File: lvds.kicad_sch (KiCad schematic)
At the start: 31 parts, among them J9 Conn_01x34_Female, U10 TPS61177A, U11 TCA9802, U12 NTB0102, U13 MIC5504-1.8YM5, U5 SN65DSI83TPAPRQ1

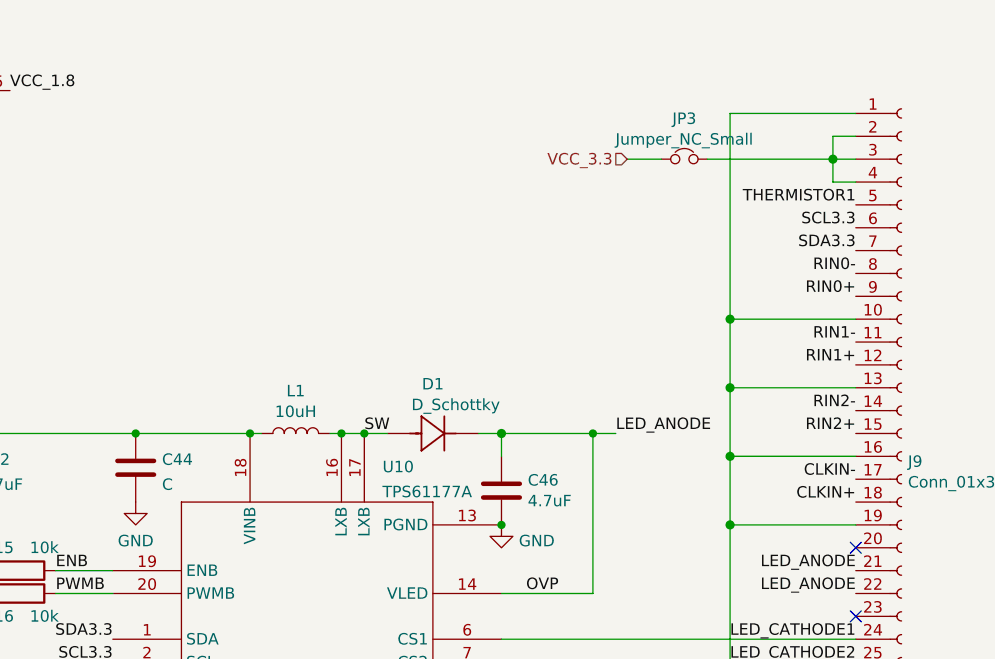
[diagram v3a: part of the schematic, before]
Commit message: Route remaining signals after rotating CM4
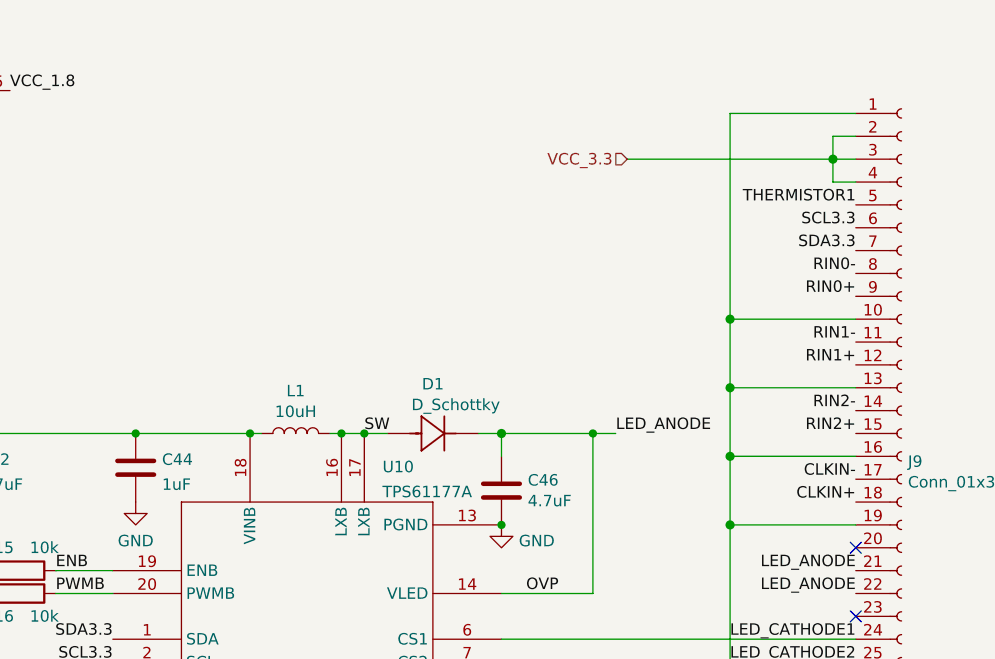
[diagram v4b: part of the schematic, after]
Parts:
- removed JP3: Jumper_NC_Small, Resistor_SMD:R_0402_1005Metric, symbol Device:Jumper_NC_Small
- C44: value C -> 1uF
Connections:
- net VCC_3.3: now also J9.2 (Pin_2), J9.3 (Pin_3), J9.4 (Pin_4)
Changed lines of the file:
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@@
-    (stroke (width 0) (type solid) (color 0 0 0 0))
-  )
-  (wire (pts (xy 236.22 34.29) (xy 240.03 34.29))
     (stroke (width 0) (type solid) (color 0 0 0 0))
   )
@@
     (stroke (width 0) (type solid) (color 0 0 0 0))
   )
-  (wire (pts (xy 245.11 34.29) (xy 259.08 34.29))
+  (wire (pts (xy 236.22 34.29) (xy 259.08 34.29))
     (stroke (width 0) (type solid) (color 0 0 0 0))
   )
@@
     )
     (property "Datasheet" "~" (id 3) (at 222.25 71.12 0)
-      (effects (font (size 1.27 1.27)) hide)
-    )
-    (pin "1")
-    (pin "2")
-  )
-  (symbol (lib_id "Device:Jumper_NC_Small") (at 242.57 34.29 0) (unit 1)
-    (in_bom yes) (on_board yes) (fields_autoplaced)
-    (property "Reference" "JP3" (id 0) (at 242.57 29.79 0))
-    (property "Value" "Jumper_NC_Small" (id 1) (at 242.57 32.0887 0))
-    (property "Footprint" "Resistor_SMD:R_0402_1005Metric" (id 2) (at 242.57 34.29 0)
-      (effects (font (size 1.27 1.27)) hide)
-    )
-    (property "Datasheet" "~" (id 3) (at 242.57 34.29 0)
       (effects (font (size 1.27 1.27)) hide)
     )
@@
       (effects (font (size 1.27 1.27)) (justify left))
     )
-    (property "Value" "C" (id 1) (at 184.531 70.4466 0)
-      (effects (font (size 1.27 1.27)) (justify left))
-    )
+    (property "Value" "1uF" (id 1) (at 184.531 70.4466 0)
+      (effects (font (size 1.27 1.27)) (justify left))
+    )

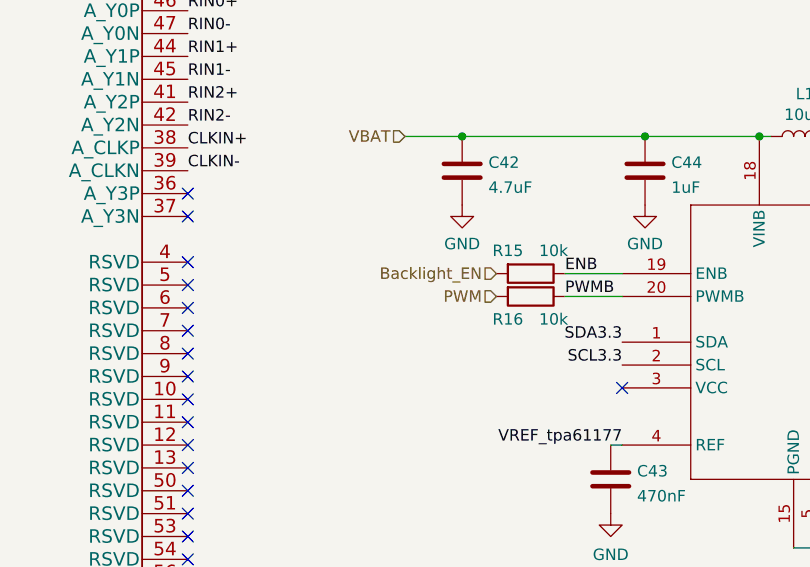
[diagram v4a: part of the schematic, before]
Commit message: Lots of tiny test points; add 3d models to a bunch of things. Re-length-match PCIe and DSI traces.
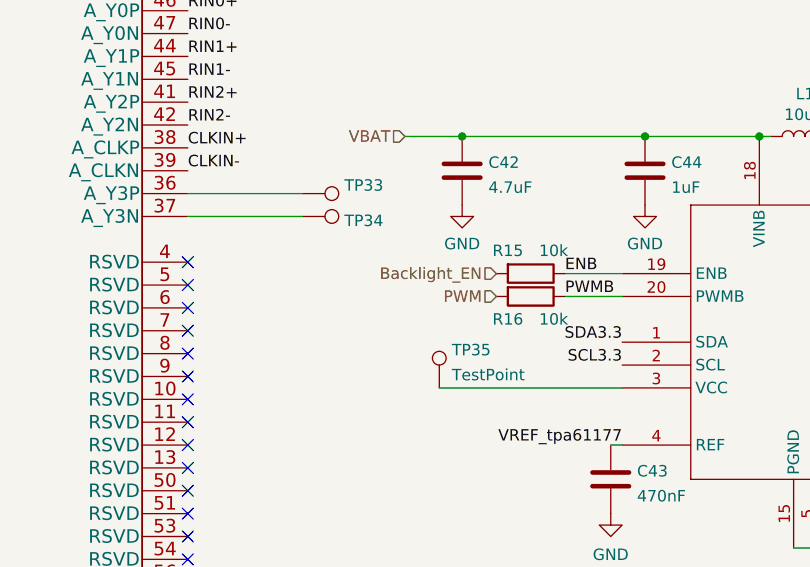
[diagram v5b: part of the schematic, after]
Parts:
- added TP33, TP34, TP35: TestPoint, footprints:testpoint_small, symbol Connector:TestPoint
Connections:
- net at U10.3 (VCC): now also TP35.1
- net at U5.36 (A_Y3P): now also TP33.1
- net at U5.37 (A_Y3N): now also TP34.1
- no-connect marks 28 -> 25
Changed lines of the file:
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@@
   (no_connect (at 130.81 124.46))
   (no_connect (at 130.81 127))
-  (no_connect (at 179.07 92.71))
   (no_connect (at 90.17 137.16))
   (no_connect (at 90.17 139.7))
   (no_connect (at 261.62 77.47))
   (no_connect (at 26.67 125.73))
-  (no_connect (at 130.81 71.12))
-  (no_connect (at 130.81 73.66))
   (wire (pts (xy 201.93 110.49) (xy 203.2 110.49))
     (stroke (width 0) (type default) (color 0 0 0 0))
@@
     (stroke (width 0) (type solid) (color 0 0 0 0))
   )
+  (wire (pts (xy 130.81 71.12) (xy 143.51 71.12))
+    (stroke (width 0) (type default) (color 0 0 0 0))
+  )
   (wire (pts (xy 232.41 64.77) (xy 232.41 82.55))
     (stroke (width 0) (type solid) (color 0 0 0 0))
@@
     (stroke (width 0) (type default) (color 0 0 0 0))
   )
+  (wire (pts (xy 158.75 92.71) (xy 179.07 92.71))
+    (stroke (width 0) (type default) (color 0 0 0 0))
+  )
   (wire (pts (xy 161.29 64.77) (xy 181.61 64.77))
     (stroke (width 0) (type default) (color 0 0 0 0))
@@
     (stroke (width 0) (type solid) (color 0 0 0 0))
   )
+  (wire (pts (xy 130.81 73.66) (xy 143.51 73.66))
+    (stroke (width 0) (type default) (color 0 0 0 0))
+  )
   (wire (pts (xy 201.93 110.49) (xy 201.93 113.03))
     (stroke (width 0) (type default) (color 0 0 0 0))
@@
     (pin "1")
     (pin "2")
+  )
+  (symbol (lib_id "Connector:TestPoint") (at 143.51 71.12 270) (unit 1)
+    (in_bom yes) (on_board yes)
+    (property "Reference" "TP33" (id 0) (at 148.209 70.2115 90)
+      (effects (font (size 1.27 1.27)) (justify left))
+    )
+    (property "Value" "TestPoint" (id 1) (at 152.4 69.85 90)
+      (effects (font (size 1.27 1.27)) (justify left) hide)
+    )
+    (property "Footprint" "footprints:testpoint_small" (id 2) (at 143.51 76.2 0)
+      (effects (font (size 1.27 1.27)) hide)
+    )
+    (property "Datasheet" "~" (id 3) (at 143.51 76.2 0)
+      (effects (font (size 1.27 1.27)) hide)
+    )
+    (pin "1")
   )
   (symbol (lib_id "Device:C") (at 35.56 25.4 0) (unit 1)
@@
     (pin "1")
   )
+  (symbol (lib_id "Connector:TestPoint") (at 158.75 92.71 0) (unit 1)
+    (in_bom yes) (on_board yes) (fields_autoplaced)
+    (property "Reference" "TP35" (id 0) (at 160.147 88.4995 0)
+      (effects (font (size 1.27 1.27)) (justify left))
+    )
+    (property "Value" "TestPoint" (id 1) (at 160.147 91.2746 0)
+      (effects (font (size 1.27 1.27)) (justify left))
+    )
+    (property "Footprint" "footprints:testpoint_small" (id 2) (at 163.83 92.71 0)
+      (effects (font (size 1.27 1.27)) hide)
+    )
+    (property "Datasheet" "~" (id 3) (at 163.83 92.71 0)
+      (effects (font (size 1.27 1.27)) hide)
+    )
+    (pin "1")
+  )
   (symbol (lib_id "power:GND") (at 181.61 72.39 0) (unit 1)
     (in_bom yes) (on_board yes) (fields_autoplaced)
@@
       (effects (font (size 1.27 1.27)) hide)
     )
-    (property "Datasheet" "" (id 3) (at 201.93 87.63 0)
+    (property "Datasheet" "${KIPRJMOD}/datasheets/tps61177a.pdf" (id 3) (at 201.93 87.63 0)
       (effects (font (size 1.27 1.27)) hide)
     )
@@
     (pin "2")
   )
+  (symbol (lib_id "Connector:TestPoint") (at 143.51 73.66 270) (unit 1)
+    (in_bom yes) (on_board yes) (fields_autoplaced)
+    (property "Reference" "TP34" (id 0) (at 148.209 74.139 90)
+      (effects (font (size 1.27 1.27)) (justify left))
+    )
+    (property "Value" "TestPoint" (id 1) (at 148.209 75.5266 90)
+      (effects (font (size 1.27 1.27)) (justify left) hide)
+    )
+    (property "Footprint" "footprints:testpoint_small" (id 2) (at 143.51 78.74 0)
+      (effects (font (size 1.27 1.27)) hide)
+    )
+    (property "Datasheet" "~" (id 3) (at 143.51 78.74 0)
+      (effects (font (size 1.27 1.27)) hide)
+    )
+    (pin "1")
+  )
   (symbol (lib_id "power:GND") (at 77.47 29.21 0) (unit 1)

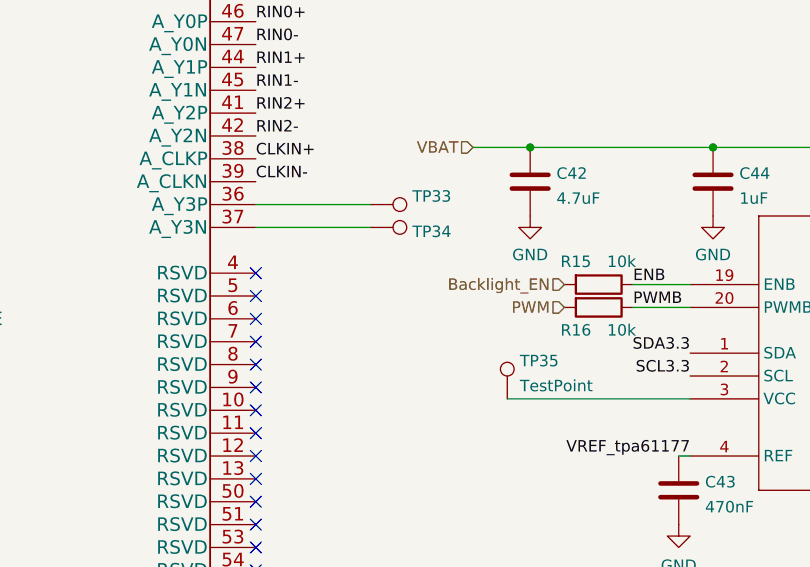
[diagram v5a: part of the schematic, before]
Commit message: Add a bunch more 3d models
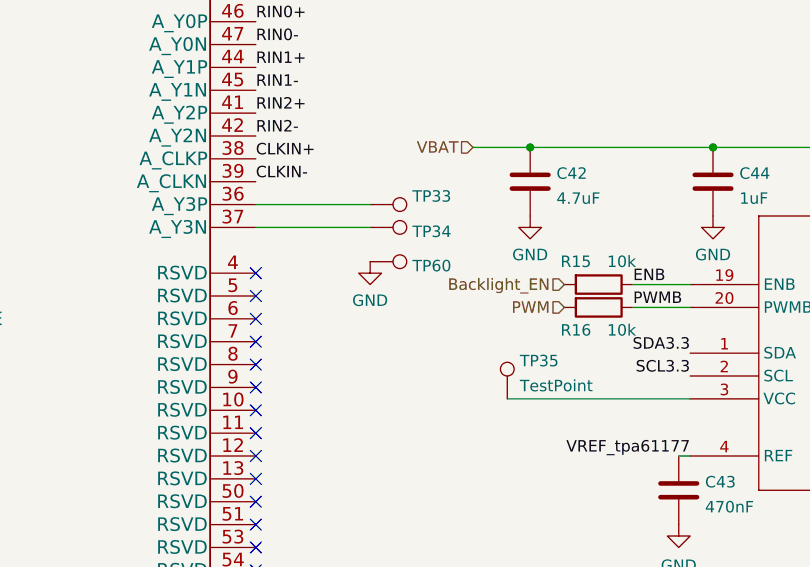
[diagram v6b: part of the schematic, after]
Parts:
- added TP60: TestPoint, footprints:testpoint_small, symbol Connector:TestPoint
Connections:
- net GND: now also TP60.1
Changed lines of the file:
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@@
     (pin "2")
+  )
+  (symbol (lib_id "Connector:TestPoint") (at 143.51 77.47 270) (unit 1)
+    (in_bom yes) (on_board yes) (fields_autoplaced)
+    (property "Reference" "TP60" (id 0) (at 148.209 77.949 90)
+      (effects (font (size 1.27 1.27)) (justify left))
+    )
+    (property "Value" "TestPoint" (id 1) (at 148.209 79.3366 90)
+      (effects (font (size 1.27 1.27)) (justify left) hide)
+    )
+    (property "Footprint" "footprints:testpoint_small" (id 2) (at 143.51 82.55 0)
+      (effects (font (size 1.27 1.27)) hide)
+    )
+    (property "Datasheet" "~" (id 3) (at 143.51 82.55 0)
+      (effects (font (size 1.27 1.27)) hide)
+    )
+    (pin "1")
   )
   (symbol (lib_id "Device:C") (at 96.52 25.4 0) (unit 1)
@@
     (pin "9")
   )
+  (symbol (lib_id "power:GND") (at 143.51 77.47 0) (unit 1)
+    (in_bom yes) (on_board yes) (fields_autoplaced)
+    (property "Reference" "#PWR030" (id 0) (at 143.51 83.82 0)
+      (effects (font (size 1.27 1.27)) hide)
+    )
+    (property "Value" "GND" (id 1) (at 143.51 81.7944 0))
+    (property "Footprint" "" (id 2) (at 143.51 77.47 0)
+      (effects (font (size 1.27 1.27)) hide)
+    )
+    (property "Datasheet" "" (id 3) (at 143.51 77.47 0)
+      (effects (font (size 1.27 1.27)) hide)
+    )
+    (pin "1")
+  )
   (symbol (lib_id "Device:C") (at 50.8 25.4 0) (unit 1)

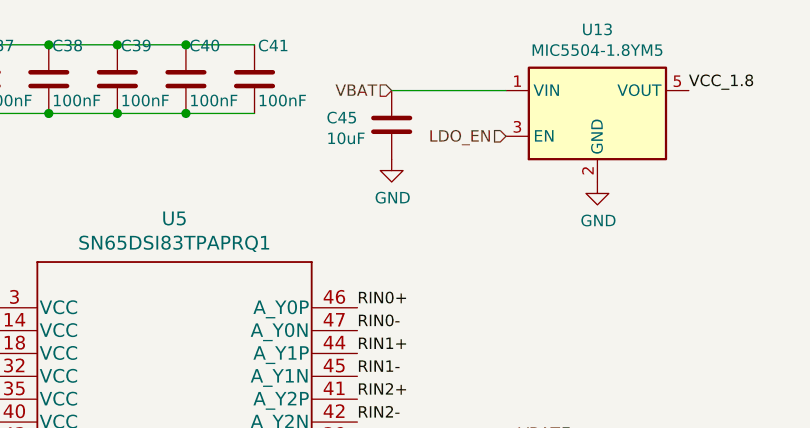
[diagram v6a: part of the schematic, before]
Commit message: Flip J4 to back of board to reduce overall thickness in that area; re-route a whole bunch of signals to accomodate that.
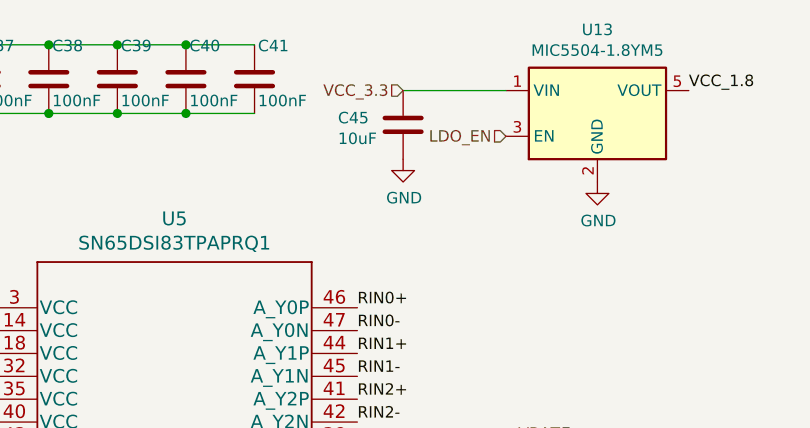
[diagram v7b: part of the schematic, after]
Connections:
- net VBAT: no longer C45.1, U13.1 (VIN)
- net VCC_3.3: now also C45.1, U13.1 (VIN)
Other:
- moved on the sheet: C45
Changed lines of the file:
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@@
     (stroke (width 0) (type default) (color 0 0 0 0))
   )
-  (wire (pts (xy 134.62 26.67) (xy 147.32 26.67))
+  (wire (pts (xy 135.89 26.67) (xy 147.32 26.67))
     (stroke (width 0) (type solid) (color 0 0 0 0))
   )
@@
     (effects (font (size 1.27 1.27)) (justify right))
   )
-  (hierarchical_label "VBAT" (shape input) (at 134.62 26.67 180)
-    (effects (font (size 1.27 1.27)) (justify right))
-  )
   (hierarchical_label "DSI1_D3_N" (shape input) (at 39.37 68.58 180)
     (effects (font (size 1.27 1.27)) (justify right))
@@
   )
   (hierarchical_label "SN65DSI83_EN" (shape input) (at 34.29 168.91 180)
+    (effects (font (size 1.27 1.27)) (justify right))
+  )
+  (hierarchical_label "VCC_3.3" (shape input) (at 135.89 26.67 180)
     (effects (font (size 1.27 1.27)) (justify right))
   )
@@
     (pin "2")
   )
-  (symbol (lib_id "Device:C") (at 134.62 30.48 0) (unit 1)
-    (in_bom yes) (on_board yes)
-    (property "Reference" "C45" (id 0) (at 127.3811 29.7191 0)
-      (effects (font (size 1.27 1.27)) (justify left))
-    )
-    (property "Value" "10uF" (id 1) (at 127.3811 32.0178 0)
-      (effects (font (size 1.27 1.27)) (justify left))
-    )
-    (property "Footprint" "Capacitor_SMD:C_0402_1005Metric" (id 2) (at 135.5852 34.29 0)
-      (effects (font (size 1.27 1.27)) hide)
-    )
-    (property "Datasheet" "~" (id 3) (at 134.62 30.48 0)
+  (symbol (lib_id "Device:C") (at 135.89 30.48 0) (unit 1)
+    (in_bom yes) (on_board yes)
+    (property "Reference" "C45" (id 0) (at 128.6511 29.7191 0)
+      (effects (font (size 1.27 1.27)) (justify left))
+    )
+    (property "Value" "10uF" (id 1) (at 128.6511 32.0178 0)
+      (effects (font (size 1.27 1.27)) (justify left))
+    )
+    (property "Footprint" "Capacitor_SMD:C_0402_1005Metric" (id 2) (at 136.8552 34.29 0)
+      (effects (font (size 1.27 1.27)) hide)
+    )
+    (property "Datasheet" "~" (id 3) (at 135.89 30.48 0)
       (effects (font (size 1.27 1.27)) hide)
     )
@@
     (pin "2")
   )
-  (symbol (lib_id "power:GND") (at 134.62 34.29 0) (unit 1)
-    (in_bom yes) (on_board yes)
-    (property "Reference" "#PWR019" (id 0) (at 134.62 40.64 0)
-      (effects (font (size 1.27 1.27)) hide)
-    )
-    (property "Value" "GND" (id 1) (at 134.7343 38.6144 0))
-    (property "Footprint" "" (id 2) (at 134.62 34.29 0)
-      (effects (font (size 1.27 1.27)) hide)
-    )
-    (property "Datasheet" "" (id 3) (at 134.62 34.29 0)
-      (effects (font (size 1.27 1.27)) hide)
-    )
+  (symbol (lib_id "power:GND") (at 135.89 34.29 0) (unit 1)
+    (in_bom yes) (on_board yes)
+    (property "Reference" "#PWR019" (id 0) (at 135.89 40.64 0)
+      (effects (font (size 1.27 1.27)) hide)
+    )
+    (property "Value" "GND" (id 1) (at 136.0043 38.6144 0))
+    (property "Footprint" "" (id 2) (at 135.89 34.29 0)
+      (effects (font (size 1.27 1.27)) hide)
+    )
+    (property "Datasheet" "" (id 3) (at 135.89 34.29 0)
+      (effects (font (size 1.27 1.27)) hide)
+    )

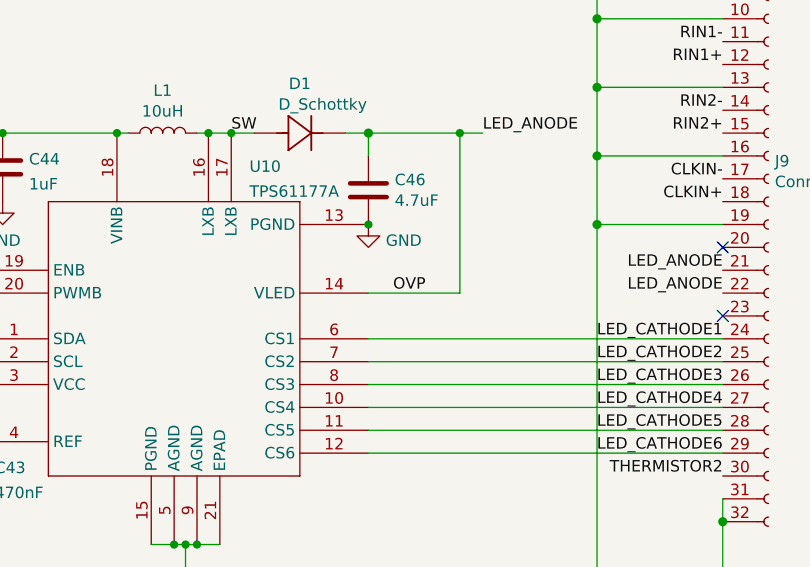
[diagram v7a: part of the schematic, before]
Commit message: Fix most ERC errors; cleanup silkscreen and comment layers.
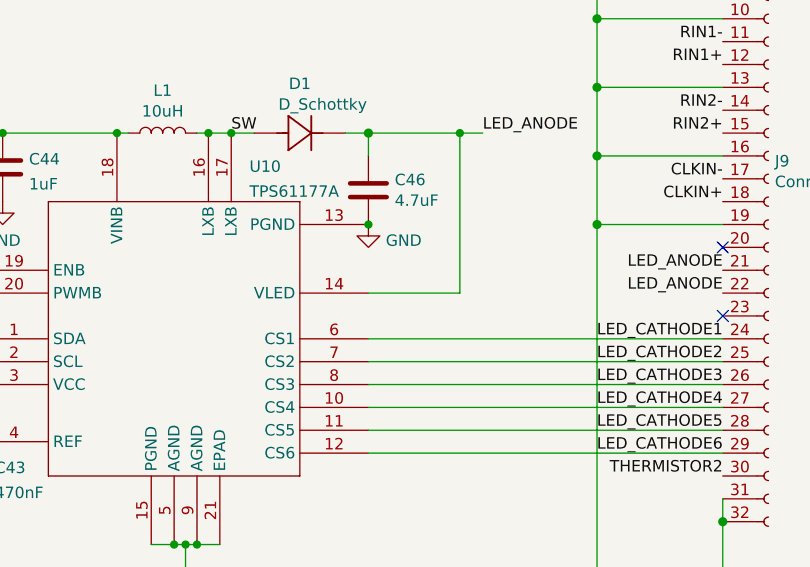
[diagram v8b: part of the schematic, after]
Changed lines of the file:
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@@
     (effects (font (size 1.27 1.27)) (justify left bottom))
-  )
-  (label "OVP" (at 228.6 82.55 180)
-    (effects (font (size 1.27 1.27)) (justify right bottom))
   )
   (label "SDA3.3" (at 179.07 87.63 180)
